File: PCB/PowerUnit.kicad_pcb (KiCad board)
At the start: 4 copper layers, 165 x 67.6 mm, 136 parts, among them J1 MX150-20, J2 MX150-20, J3 MX150-8, J4 REDCUBE, J5 CON-3, Q1 BC847C, Q10 STD45P4LLF6AG, Q11 STD45P4LLF6AG, Q12 STD15P6F6AG, Q13 STD15P6F6AG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

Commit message: Added revision
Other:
- board text added: "Prod. 110000 Rev. A"
- board text removed: "110000"
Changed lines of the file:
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@@
   (gr_line (start 55.39 151.47) (end 56.2 152.63) (layer Edge.Cuts) (width 0.05))
   (gr_line (start 55.39 150) (end 55.39 151.47) (layer Edge.Cuts) (width 0.05))
-  (gr_text 110000 (at 213 112.5 90) (layer F.SilkS)
+  (gr_text "Prod. 110000 Rev. A" (at 213 112.5 90) (layer F.SilkS)
     (effects (font (size 2 2) (thickness 0.3)))
   )

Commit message: fix Fab
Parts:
- C10, C11, C12, C13, C2, C3, C5, C6, C7, C8: value 10n -> 100n
- R1, R14, R15, R16, R19, R2, R20, R24, R25, R26, R27, R3, R39, R4, R8: value 2.2k -> 1k
- R10, R11, R12, R17, R18, R21, R22, R23, R7, R9: value 820 -> 1k

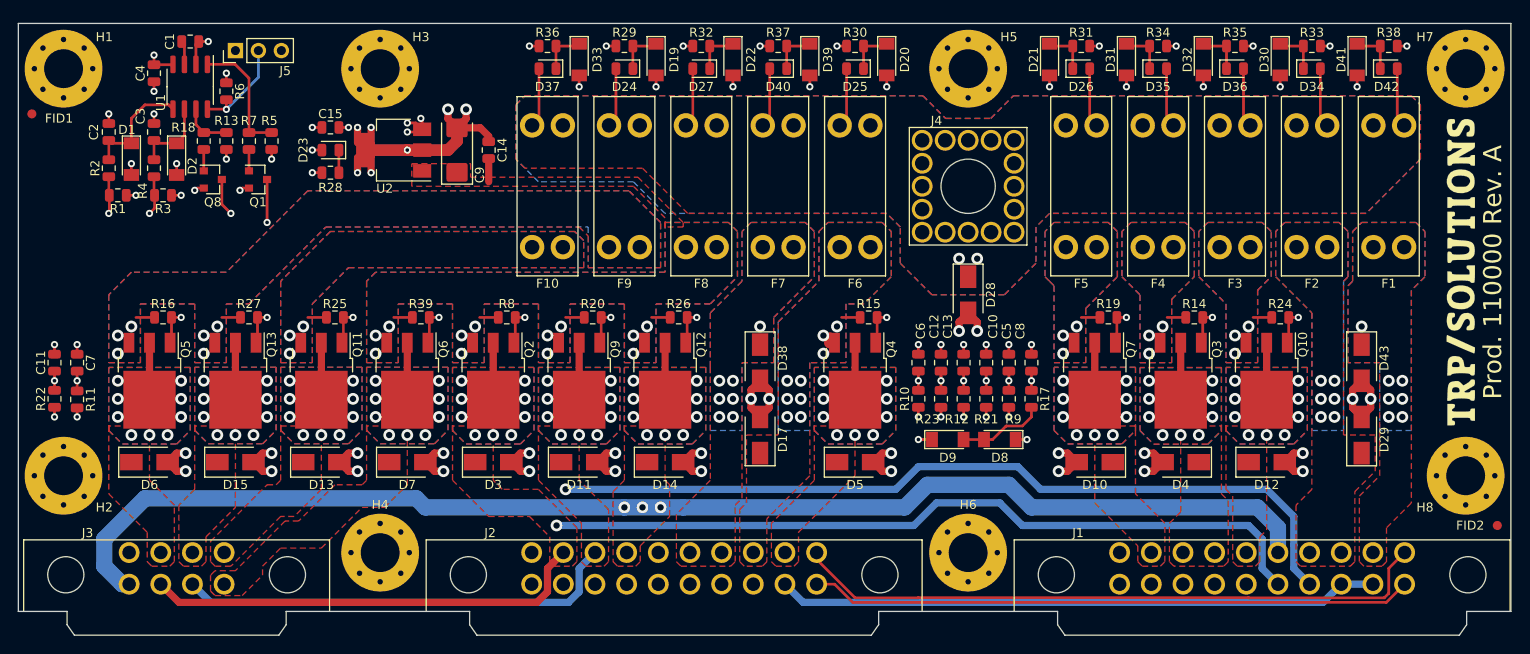
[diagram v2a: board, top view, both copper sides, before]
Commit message: remove resistors / New layout
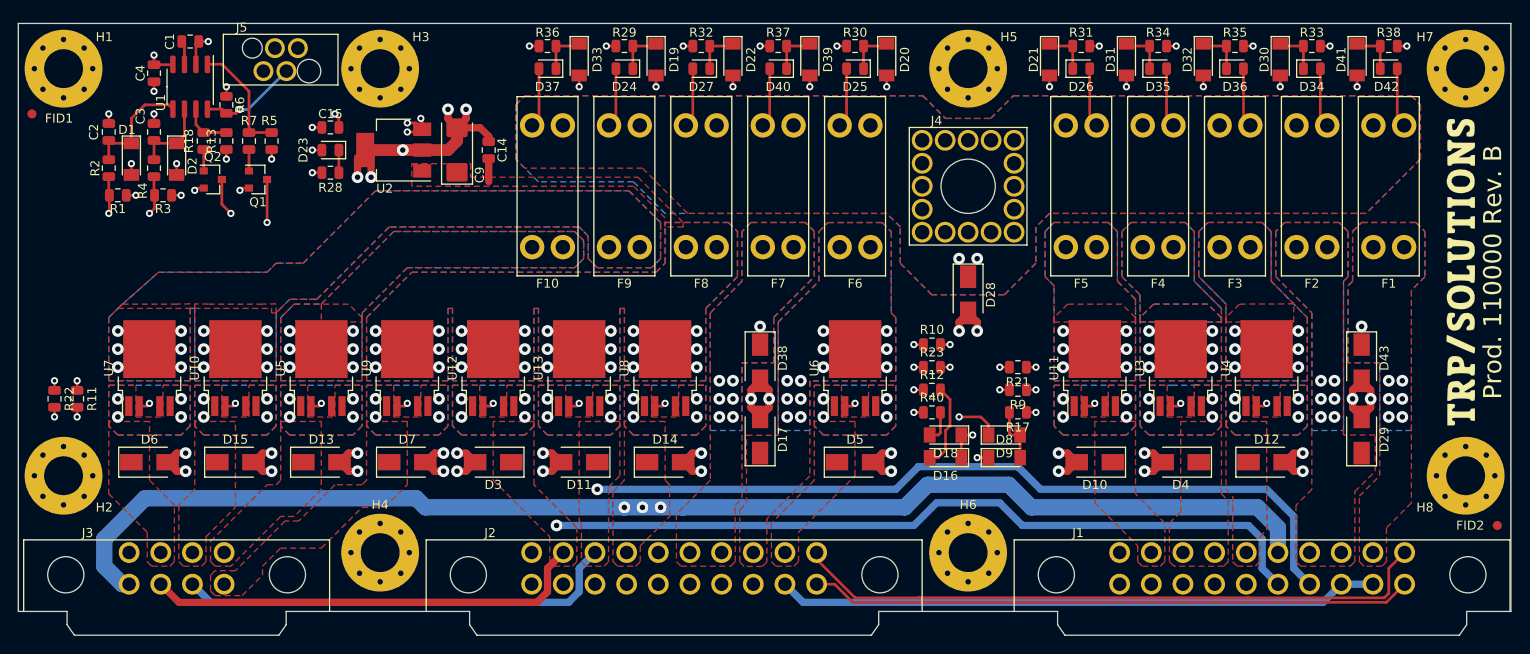
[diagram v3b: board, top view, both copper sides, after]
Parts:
- removed C10, C11, C12, C13, C5, C6, C7, C8: 100n, erp:C_0805_2012Metric
- removed Q10, Q11, Q3, Q4, Q7: STD45P4LLF6AG, erp:TO-252-3_TabPin2
- removed Q12, Q13, Q5, Q6, Q9: STD15P6F6AG, erp:TO-252-3_TabPin2
- removed Q8: BC847C, erp:SOT-23
- removed R14, R15, R16, R19, R20, R24, R25, R26, R27, R39, R8: 1k, erp:R_0805_2012Metric
- added D16: LL4148, erp:D_MiniMELF, F.Cu at (152.5, 133.0)
- added D18: LL4148, erp:D_MiniMELF, F.Cu at (152.5, 130.5)
- added R40: 100, erp:R_0805_2012Metric, F.Cu at (151.0, 128.0)
- added U10: BTS6143D, erp:TO-252-5_TabPin3X, F.Cu at (74.0, 123.1)
- added U11: BTS6143D, erp:TO-252-5_TabPin3X, F.Cu at (169.0, 123.1)
- added U12: BTS6143D, erp:TO-252-5_TabPin3X, F.Cu at (102.5, 123.1)
- added U13: BTS6143D, erp:TO-252-5_TabPin3X, F.Cu at (112.0, 123.1)
- added U3: BTS6143D, erp:TO-252-5_TabPin3X, F.Cu at (178.5, 123.1)
- added U4: BTS6143D, erp:TO-252-5_TabPin3X, F.Cu at (188.0, 123.1)
- added U5: BTS6143D, erp:TO-252-5_TabPin3X, F.Cu at (83.5, 123.1)
- added U6: BTS6143D, erp:TO-252-5_TabPin3X, F.Cu at (142.5, 123.1)
- added U7: BTS6143D, erp:TO-252-5_TabPin3X, F.Cu at (64.5, 123.1)
- added U8: BTS6143D, erp:TO-252-5_TabPin3X, F.Cu at (121.5, 123.1)
- added U9: BTS6143D, erp:TO-252-5_TabPin3X, F.Cu at (93.0, 123.1)
- J5: value CON-3 -> REDFIT-4; footprint erp:PinHeader_1x03_P2.54mm_Vertical -> erp:Wurth_WR-WST_IDC_4
- Q2: value STD15P6F6AG -> BC847C; footprint erp:TO-252-3_TabPin2 -> erp:SOT-23
- R10, R11, R12, R17, R21, R22, R23, R9: value 1k -> 100
- moved Q2 38.2 mm to (71.5, 102.2), turned to 0 degrees
- moved D9 6.27 mm to (159.0, 130.5)
- moved R10 6.18 mm to (151.0, 120.5), turned to 0 degrees
- moved J5 5.10 mm to (79.0, 89.0), turned to 0 degrees
- moved R21 4.95 mm to (160.5, 123.0), turned to 180 degrees
- moved R12 3.64 mm to (151.0, 125.5), turned to 0 degrees
- moved R23 3.64 mm to (151.0, 123.0), turned to 0 degrees
- moved R17 2.12 mm to (160.5, 128.0), turned to 180 degrees
- moved D8 2.06 mm to (159.0, 133.0), turned to 0 degrees
- moved R6 1.50 mm to (73.0, 94.0)
- moved R9 1.41 mm to (160.5, 125.5), turned to 180 degrees
- moved R11 0.06 mm to (56.5, 126.5)
- turned D11 to 180 degrees
- turned D3 to 180 degrees
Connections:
- J1 pad 11: (no net) -> Net-(J1-Pad11)
- J1 pad 12: (no net) -> Net-(J1-Pad12)
- J2 pad 11: (no net) -> Net-(J2-Pad11)
- J5 pad 1: GND -> +5V
- J5 pad 3: +5V -> GND
- Q2 pad 1: Net-(Q1-Pad3) -> Net-(Q2-Pad1)
- Q2 pad 2: /OUT_LEFT -> GND
- Q2 pad 3: /PWD_LIGHT -> Net-(Q2-Pad3)
- R12 pad 2: /IN_BRAKE -> Net-(D16-Pad2)
- R18 pad 1: Net-(Q8-Pad1) -> Net-(Q2-Pad1)
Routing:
- net Net-(R40-Pad1): track 0.00 -> 80.8 mm, vias 0 -> 2
- net Net-(Q8-Pad3): track 54.9 -> 0.00 mm, vias 2 -> 0
- net Net-(Q2-Pad3): track 0.00 -> 54.4 mm, vias 0 -> 2
- net Net-(R12-Pad1): track 95.8 -> 63.3 mm, vias 3 -> 2
- net Net-(R21-Pad1): track 46.5 -> 29.5 mm
- net Net-(R9-Pad1): track 34.9 -> 19.4 mm
- net GND: track 145.9 -> 133.4 mm, vias 66 -> 56
- net Net-(R17-Pad1): track 23.4 -> 10.9 mm
- net Net-(R22-Pad1): track 45.8 -> 33.5 mm
- net Net-(R11-Pad1): track 21.7 -> 11.4 mm
- net /OUT_RIGHT: track 148.2 -> 138.4 mm, vias 10 -> 5
- net /IN_AUX: track 39.0 -> 48.4 mm
- net Net-(D16-Pad2): track 0.00 -> 9.43 mm
- net /PWD_LIGHT: track 31.0 -> 22.7 mm, vias 13 -> 25
- net /IN_FAN_B: track 34.4 -> 42.0 mm
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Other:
- board text added: "Prod. 110000 Rev. B"
- board text removed: "Prod. 110000 Rev. A"
